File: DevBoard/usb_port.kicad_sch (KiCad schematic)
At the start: 105 parts, among them J501 TYPE-C 16PCB0.8 IP68, J502 I2CC logic analyzer, Q501 IAUC45N04S6L063H, Q502 IAUC45N04S6L063H, U501 TPS25751DREFR, U502 M24512-DFMC6TG, U503 BQ25756RRVR, U504 TPS62933DRLR

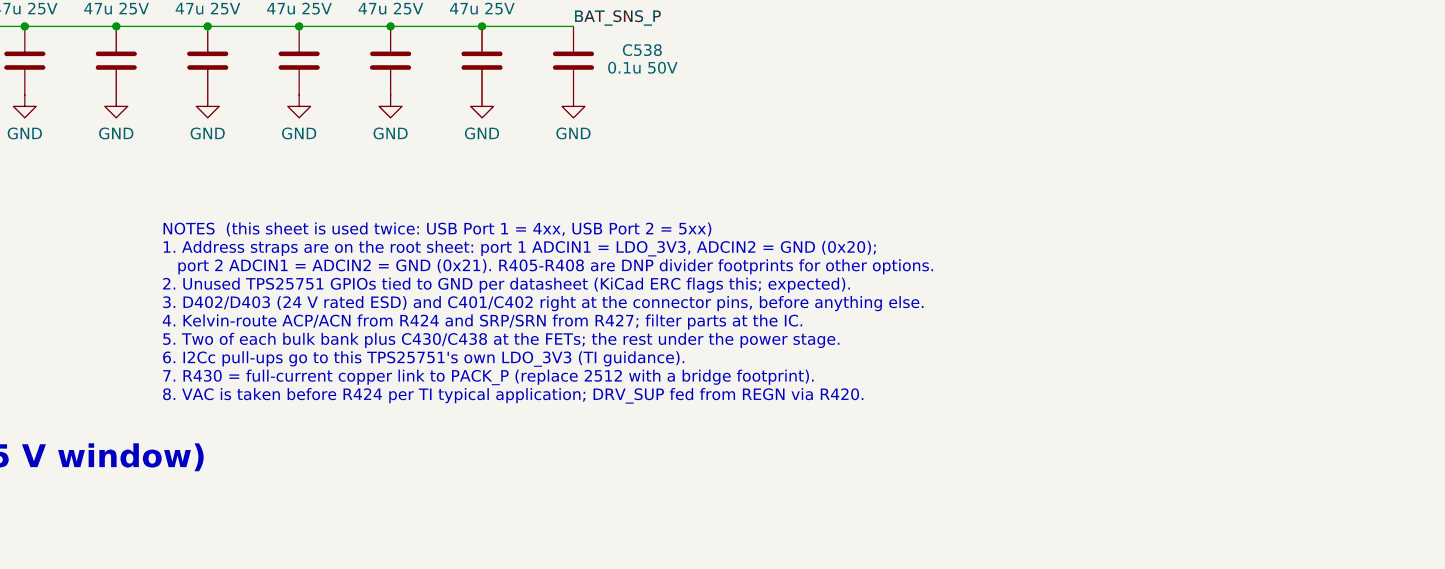
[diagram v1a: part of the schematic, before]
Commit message: Dev board: hand-solder the INA190s, keep PPHV bulk with soft-start
- U201/U202 sourced from DigiKey/Mouser and hand-soldered: excluded from the
  position file, LCSC removed, MPN and Sourcing properties added, sheet note
- PPHV bulk above 100 uF justified by the TPS25751D sink soft-start (inrush
  ~0.1 A at setting 0); sheet note asks for SS setting 0 or 1 in config
- README and circuit description updated

Co-Authored-By: Claude Opus 5.5 <noreply@anthropic.com>
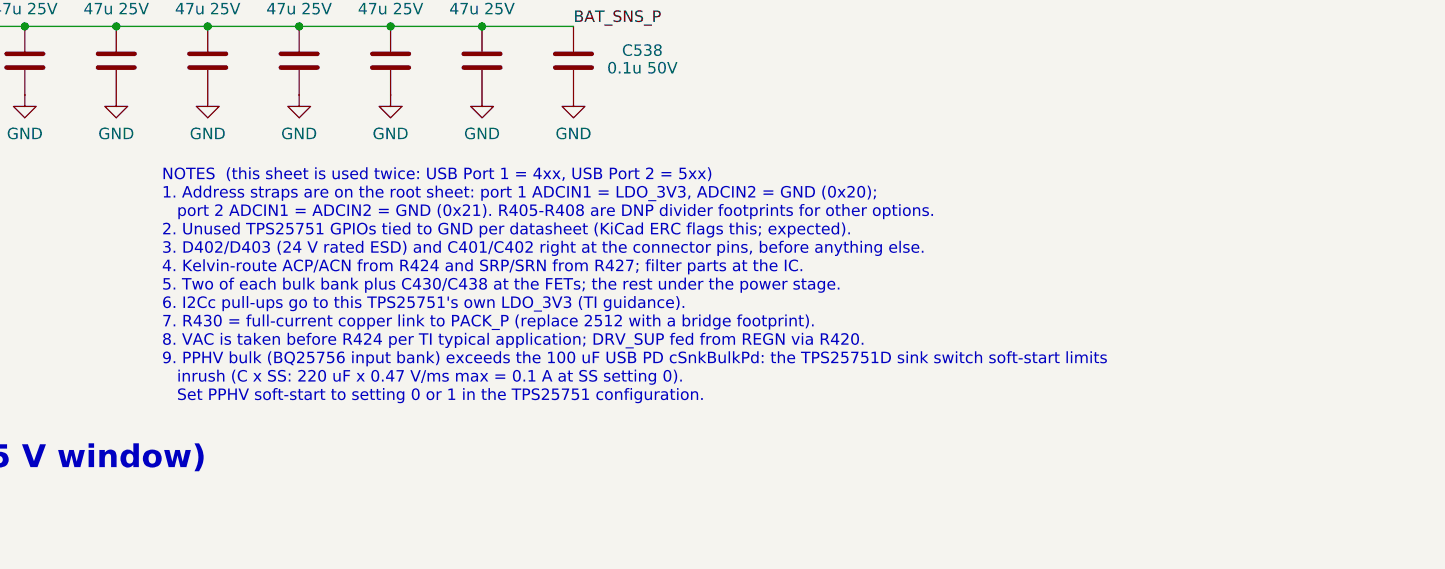
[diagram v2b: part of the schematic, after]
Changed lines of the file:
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@@
 		)
 	)
-	(text "NOTES  (this sheet is used twice: USB Port 1 = 4xx, USB Port 2 = 5xx)\n1. Address straps are on the root sheet: port 1 ADCIN1 = LDO_3V3, ADCIN2 = GND (0x20);\n   port 2 ADCIN1 = ADCIN2 = GND (0x21). R405-R408 are DNP divider footprints for other options.\n2. Unused TPS25751 GPIOs tied to GND per datasheet (KiCad ERC flags this; expected).\n3. D402/D403 (24 V rated ESD) and C401/C402 right at the connector pins, before anything else.\n4. Kelvin-route ACP/ACN from R424 and SRP/SRN from R427; filter parts at the IC.\n5. Two of each bulk bank plus C430/C438 at the FETs; the rest under the power stage.\n6. I2Cc pull-ups go to this TPS25751's own LDO_3V3 (TI guidance).\n7. R430 = full-current copper link to PACK_P (replace 2512 with a bridge footprint).\n8. VAC is taken before R424 per TI typical application; DRV_SUP fed from REGN via R420."
+	(text "NOTES  (this sheet is used twice: USB Port 1 = 4xx, USB Port 2 = 5xx)\n1. Address straps are on the root sheet: port 1 ADCIN1 = LDO_3V3, ADCIN2 = GND (0x20);\n   port 2 ADCIN1 = ADCIN2 = GND (0x21). R405-R408 are DNP divider footprints for other options.\n2. Unused TPS25751 GPIOs tied to GND per datasheet (KiCad ERC flags this; expected).\n3. D402/D403 (24 V rated ESD) and C401/C402 right at the connector pins, before anything else.\n4. Kelvin-route ACP/ACN from R424 and SRP/SRN from R427; filter parts at the IC.\n5. Two of each bulk bank plus C430/C438 at the FETs; the rest under the power stage.\n6. I2Cc pull-ups go to this TPS25751's own LDO_3V3 (TI guidance).\n7. R430 = full-current copper link to PACK_P (replace 2512 with a bridge footprint).\n8. VAC is taken before R424 per TI typical application; DRV_SUP fed from REGN via R420.\n9. PPHV bulk (BQ25756 input bank) exceeds the 100 uF USB PD cSnkBulkPd: the TPS25751D sink switch soft-start limits\n   inrush (C x SS: 220 uF x 0.47 V/ms max = 0.1 A at SS setting 0).\n   Set PPHV soft-start to setting 0 or 1 in the TPS25751 configuration."
 		(exclude_from_sim no)
 		(at 459.74 160.02 0)
@@
 		(dnp no)
 		(property "Reference" "C546"
-			(at 76.20 191.68 0)
+			(at 76.2 191.68 0)
 			(show_name no)
 			(do_not_autoplace no)
@@
 		)
 		(property "Value" "0.1u 50V"
-			(at 76.20 193.65 0)
+			(at 76.2 193.65 0)
 			(show_name no)
 			(do_not_autoplace no)
@@
 		(dnp no)
 		(property "Reference" "C525"
-			(at 368.30 114.21 0)
+			(at 368.3 114.21 0)
 			(show_name no)
 			(do_not_autoplace no)
@@
 		)
 		(property "Value" "22u 35V"
-			(at 368.30 116.18 0)
+			(at 368.3 116.18 0)
 			(show_name no)
 			(do_not_autoplace no)
@@
 		(dnp no)
 		(property "Reference" "C543"
-			(at 157.48 199.30 0)
+			(at 157.48 199.3 0)
 			(show_name no)
 			(do_not_autoplace no)
@@
 		(dnp no)
 		(property "Reference" "C541"
-			(at 137.16 199.30 0)
+			(at 137.16 199.3 0)
 			(show_name no)
 			(do_not_autoplace no)
@@
 		)
 		(property "Value" "3V3"
-			(at 317.50 192.53 0)
+			(at 317.5 192.53 0)
 			(show_name no)
 			(do_not_autoplace no)
@@
 		)
 		(property "Value" "GND"
-			(at 38.10 123.70 0)
+			(at 38.1 123.7 0)
 			(show_name no)
 			(do_not_autoplace no)
@@
 		)
 		(property "Value" "GND"
-			(at 266.70 161.80 0)
+			(at 266.7 161.8 0)
 			(show_name no)
 			(do_not_autoplace no)
@@
 		)
 		(property "Value" "GND"
-			(at 456.00 99.06 0)
+			(at 456 99.06 0)
 			(show_name no)
 			(do_not_autoplace no)
@@
 		(dnp no)
 		(property "Reference" "U503"
-			(at 381.00 174.05 0)
+			(at 381 174.05 0)
 			(show_name no)
 			(do_not_autoplace no)
@@
 		)
 		(property "Value" "BQ25756RRVR"
-			(at 381.00 176.02 0)
+			(at 381 176.02 0)
 			(show_name no)
 			(do_not_autoplace no)
@@
 		)
 		(property "Value" "GND"
-			(at 45.72 123.70 0)
+			(at 45.72 123.7 0)
 			(show_name no)
 			(do_not_autoplace no)
@@
 		(dnp no)
 		(property "Reference" "R519"
-			(at 419.33 213.50 0)
+			(at 419.33 213.5 0)
 			(show_name no)
 			(do_not_autoplace no)
@@
 		(dnp no)
 		(property "Reference" "U504"
-			(at 101.60 189.29 0)
+			(at 101.6 189.29 0)
 			(show_name no)
 			(do_not_autoplace no)
@@
 		)
 		(property "Value" "TPS62933DRLR"
-			(at 101.60 191.26 0)
+			(at 101.6 191.26 0)
 			(show_name no)
 			(do_not_autoplace no)
@@
 		)
 		(property "Value" "GND"
-			(at 76.20 229.11 0)
+			(at 76.2 229.11 0)
 			(show_name no)
 			(do_not_autoplace no)
@@
 		(dnp no)
 		(property "Reference" "C530"
-			(at 419.10 114.21 0)
+			(at 419.1 114.21 0)
 			(show_name no)
 			(do_not_autoplace no)
@@
 		)
 		(property "Value" "0.1u 50V"
-			(at 419.10 116.18 0)
+			(at 419.1 116.18 0)
 			(show_name no)
 			(do_not_autoplace no)
@@
 		(dnp no)
 		(property "Reference" "C532"
-			(at 444.50 114.21 0)
+			(at 444.5 114.21 0)
 			(show_name no)
 			(do_not_autoplace no)
@@
 		)
 		(property "Value" "47u 25V"
-			(at 444.50 116.18 0)
+			(at 444.5 116.18 0)
 			(show_name no)
 			(do_not_autoplace no)
@@
 		)
 		(property "Value" "GND"
-			(at 368.30 130.05 0)
+			(at 368.3 130.05 0)
 			(show_name no)
 			(do_not_autoplace no)
@@
 		(dnp no)
 		(property "Reference" "C517"
-			(at 458.20 85.38 90)
+			(at 458.2 85.38 90)
 			(show_name no)
 			(do_not_autoplace no)
@@
 		)
 		(property "Value" "0.47u 25V"
-			(at 458.20 87.34 90)
+			(at 458.2 87.34 90)
 			(show_name no)
 			(do_not_autoplace no)
@@
 		)
 		(property "Value" "GND"
-			(at 363.22 85.60 0)
+			(at 363.22 85.6 0)
 			(show_name no)
 			(do_not_autoplace no)
@@
 		(dnp no)
 		(property "Reference" "J502"
-			(at 284.48 161.80 0)
+			(at 284.48 161.8 0)
 			(show_name no)
 			(do_not_autoplace no)
@@
 		)
 		(property "Value" "GND"
-			(at 495.30 130.05 0)
+			(at 495.3 130.05 0)
 			(show_name no)
 			(do_not_autoplace no)
@@
 		)
 		(property "Value" "GND"
-			(at 317.50 130.05 0)
+			(at 317.5 130.05 0)
 			(show_name no)
 			(do_not_autoplace no)
@@
 		(dnp no)
 		(property "Reference" "R511"
-			(at 342.67 200.80 0)
+			(at 342.67 200.8 0)
 			(show_name no)
 			(do_not_autoplace no)
@@
 		(dnp no)
 		(property "Reference" "C537"
-			(at 495.30 114.21 0)
+			(at 495.3 114.21 0)
 			(show_name no)
 			(do_not_autoplace no)
@@
 		)
 		(property "Value" "47u 25V"
-			(at 495.30 116.18 0)
+			(at 495.3 116.18 0)
 			(show_name no)
 			(do_not_autoplace no)
@@
 		)
 		(property "Value" "GND"
-			(at 254.00 164.34 0)
+			(at 254 164.34 0)
 			(show_name no)
 			(do_not_autoplace no)
@@
 		)
 		(property "Value" "GND"
-			(at 354.40 208.28 0)
+			(at 354.4 208.28 0)
 			(show_name no)
 			(do_not_autoplace no)
@@
 		)
 		(property "Value" "IAUC45N04S6L063H"
-			(at 350.52 66.80 0)
+			(at 350.52 66.8 0)
 			(show_name no)
 			(do_not_autoplace no)
@@
 		)
 		(property "Value" "PWR_FLAG"
-			(at 228.60 285.24 0)
+			(at 228.6 285.24 0)
 			(show_name no)
 			(do_not_autoplace no)
@@
 		(dnp no)
 		(property "Reference" "R513"
-			(at 353.06 244.20 0)
+			(at 353.06 244.2 0)
 			(show_name no)
 			(do_not_autoplace no)
@@
 		(dnp no)
 		(property "Reference" "Q502"
-			(at 419.10 64.83 0)
+			(at 419.1 64.83 0)
 			(show_name no)
 			(do_not_autoplace no)
@@
 		)
 		(property "Value" "IAUC45N04S6L063H"
-			(at 419.10 66.80 0)
+			(at 419.1 66.8 0)
 			(show_name no)
 			(do_not_autoplace no)
@@
 		)
 		(property "Value" "10k B3435"
-			(at 410.78 238.10 0)
+			(at 410.78 238.1 0)
 			(show_name no)
 			(do_not_autoplace no)
@@
 		(dnp no)
 		(property "Reference" "C540"
-			(at 114.30 204.83 0)
+			(at 114.3 204.83 0)
 			(show_name no)
 			(do_not_autoplace no)
@@
 		)
 		(property "Value" "0.1u 25V"
-			(at 114.30 206.80 0)
+			(at 114.3 206.8 0)
 			(show_name no)
 			(do_not_autoplace no)
@@
 		)
 		(property "Value" "GND"
-			(at 406.40 85.60 0)
+			(at 406.4 85.6 0)
 			(show_name no)
 			(do_not_autoplace no)
@@
 		)
 		(property "Value" "GND"
-			(at 444.50 130.05 0)
+			(at 444.5 130.05 0)
 			(show_name no)
 			(do_not_autoplace no)
@@
 		)
 		(property "Value" "GND"
-			(at 76.20 207.52 0)
+			(at 76.2 207.52 0)
 			(show_name no)
 			(do_not_autoplace no)
@@
 		(dnp no)
 		(property "Reference" "C512"
-			(at 406.40 173.90 0)
+			(at 406.4 173.9 0)
 			(show_name no)
 			(do_not_autoplace no)
@@
 		)
 		(property "Value" "0.1u 25V"
-			(at 406.40 175.87 0)
+			(at 406.4 175.87 0)
 			(show_name no)
 			(do_not_autoplace no)
@@
 		(dnp no)
 		(property "Reference" "TP503"
-			(at 76.20 283.71 0)
+			(at 76.2 283.71 0)
 			(show_name no)
 			(do_not_autoplace no)
@@
 		(dnp no)
 		(property "Reference" "C542"
-			(at 147.32 199.30 0)
+			(at 147.32 199.3 0)
 			(show_name no)
 			(do_not_autoplace no)
@@
 		)
 		(property "Value" "GND"
-			(at 356.94 241.30 0)
+			(at 356.94 241.3 0)
 			(show_name no)
 			(do_not_autoplace no)
@@
 		)
 		(property "Value" "GND"
-			(at 342.90 244.35 0)
+			(at 342.9 244.35 0)
 			(show_name no)
 			(do_not_autoplace no)
@@
 		)
 		(property "Value" "GND"
-			(at 238.76 161.80 0)
+			(at 238.76 161.8 0)
 			(show_name no)
 			(do_not_autoplace no)
@@
 		)
 		(property "Value" "GND"
-			(at 101.60 220.22 0)
+			(at 101.6 220.22 0)
 			(show_name no)
 			(do_not_autoplace no)
@@
 		(dnp no)
 		(property "Reference" "TP508"
-			(at 152.40 283.71 0)
+			(at 152.4 283.71 0)
 			(show_name no)
 			(do_not_autoplace no)
@@
 		)
 		(property "Value" "GND"
-			(at 419.10 130.05 0)
+			(at 419.1 130.05 0)
 			(show_name no)
 			(do_not_autoplace no)

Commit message: Dev board: project footprints for holder, USB-C, half-bridge, module, EEPROM, BQ25756
- tools/make_footprints.py generates MonolithDev.pretty from the datasheets:
  BH-21700-B1BJ001 holder, Shou Han USB-C (with board-edge cutout),
  Infineon PG-TDSON-8-57 half-bridge (land + stencil), STM32WB1MMC LGA77,
  ST UFDFPN8 2x3 with the correct 1.2x1.4 exposed pad, and a 10 A net tie
- BQ25756 RRV0036A footprint from Antmicro (Apache-2.0), checked against TI
- Footprints assigned; R430/R530 become net-tie links, off the BOM and CPL
- Every symbol pin has a pad and vice versa; nets, ERC and overlaps unchanged

Co-Authored-By: Claude Opus 5.5 <noreply@anthropic.com>
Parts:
- J501: footprint (none) -> MonolithDev:USB_C_Receptacle_ShouHan_TYPE-C_16PCB0.8_IP68
- Q501, Q502: footprint (none) -> MonolithDev:Infineon_PG-TDSON-8-57_HalfBridge
- R530: value 0R copper link -> Link 10A; footprint Resistor_SMD:R_2512_6332Metric -> MonolithDev:NetTie-2_SMD_3x3mm_Bridge3mm; Notes full current -> copper link (net tie footprint), not a part; keeps VBAT_SYS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; now left out of the parts list
- U502: footprint Package_DFN_QFN:DFN-8-1EP_2x3mm_P0.5mm_EP0.61x2.2mm -> MonolithDev:ST_UFDFPN-8-1EP_2x3mm_P0.5mm_EP1.2x1.4mm
- U503: footprint (none) -> MonolithDev:TI_VQFN-36-1EP_RRV0036A_5x6mm_P0.5mm
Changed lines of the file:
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@@
 		)
 	)
-	(text "NOTES  (this sheet is used twice: USB Port 1 = 4xx, USB Port 2 = 5xx)\n1. Address straps are on the root sheet: port 1 ADCIN1 = LDO_3V3, ADCIN2 = GND (0x20);\n   port 2 ADCIN1 = ADCIN2 = GND (0x21). R405-R408 are DNP divider footprints for other options.\n2. Unused TPS25751 GPIOs tied to GND per datasheet (KiCad ERC flags this; expected).\n3. D402/D403 (24 V rated ESD) and C401/C402 right at the connector pins, before anything else.\n4. Kelvin-route ACP/ACN from R424 and SRP/SRN from R427; filter parts at the IC.\n5. Two of each bulk bank plus C430/C438 at the FETs; the rest under the power stage.\n6. I2Cc pull-ups go to this TPS25751's own LDO_3V3 (TI guidance).\n7. R430 = full-current copper link to PACK_P (replace 2512 with a bridge footprint).\n8. VAC is taken before R424 per TI typical application; DRV_SUP fed from REGN via R420.\n9. PPHV bulk (BQ25756 input bank) exceeds the 100 uF USB PD cSnkBulkPd: the TPS25751D sink switch soft-start limits\n   inrush (C x SS: 220 uF x 0.47 V/ms max = 0.1 A at SS setting 0).\n   Set PPHV soft-start to setting 0 or 1 in the TPS25751 configuration."
+	(text "NOTES  (this sheet is used twice: USB Port 1 = 4xx, USB Port 2 = 5xx)\n1. Address straps are on the root sheet: port 1 ADCIN1 = LDO_3V3, ADCIN2 = GND (0x20);\n   port 2 ADCIN1 = ADCIN2 = GND (0x21). R405-R408 are DNP divider footprints for other options.\n2. Unused TPS25751 GPIOs tied to GND per datasheet (KiCad ERC flags this; expected).\n3. D402/D403 (24 V rated ESD) and C401/C402 right at the connector pins, before anything else.\n4. Kelvin-route ACP/ACN from R424 and SRP/SRN from R427; filter parts at the IC.\n5. Two of each bulk bank plus C430/C438 at the FETs; the rest under the power stage.\n6. I2Cc pull-ups go to this TPS25751's own LDO_3V3 (TI guidance).\n7. R430 = 10 A copper link to PACK_P (net-tie footprint, not a part); widen with zones.\n8. VAC is taken before R424 per TI typical application; DRV_SUP fed from REGN via R420.\n9. PPHV bulk (BQ25756 input bank) exceeds the 100 uF USB PD cSnkBulkPd: the TPS25751D sink switch soft-start limits\n   inrush (C x SS: 220 uF x 0.47 V/ms max = 0.1 A at SS setting 0).\n   Set PPHV soft-start to setting 0 or 1 in the TPS25751 configuration."
 		(exclude_from_sim no)
 		(at 459.74 160.02 0)
@@
 			)
 		)
-		(property "Footprint" "Package_DFN_QFN:DFN-8-1EP_2x3mm_P0.5mm_EP0.61x2.2mm"
+		(property "Footprint" "MonolithDev:ST_UFDFPN-8-1EP_2x3mm_P0.5mm_EP1.2x1.4mm"
 			(at 254 152.4 0)
 			(hide yes)
@@
 			)
 		)
-		(property "Footprint" ""
+		(property "Footprint" "MonolithDev:TI_VQFN-36-1EP_RRV0036A_5x6mm_P0.5mm"
 			(at 381 203.2 0)
 			(hide yes)
@@
 		(body_style 1)
 		(exclude_from_sim no)
-		(in_bom yes)
+		(in_bom no)
 		(on_board yes)
-		(in_pos_files yes)
+		(in_pos_files no)
 		(dnp no)
 		(property "Reference" "R530"
@@
 			)
 		)
-		(property "Value" "0R copper link"
+		(property "Value" "Link 10A"
 			(at 474.83 58.16 90)
 			(show_name no)
@@
 			)
 		)
-		(property "Footprint" "Resistor_SMD:R_2512_6332Metric"
+		(property "Footprint" "MonolithDev:NetTie-2_SMD_3x3mm_Bridge3mm"
 			(at 474.98 62.738 90)
 			(hide yes)
@@
 			)
 		)
-		(property "Notes" "full current"
+		(property "Notes" "copper link (net tie footprint), not a part; keeps VBAT_SYS and PACK_P as separate net names"
 			(at 0 0 0)
 			(hide yes)
@@
 			)
 		)
-		(property "Footprint" ""
+		(property "Footprint" "MonolithDev:Infineon_PG-TDSON-8-57_HalfBridge"
 			(at 350.52 73.66 0)
 			(hide yes)
@@
 			)
 		)
-		(property "Footprint" ""
+		(property "Footprint" "MonolithDev:Infineon_PG-TDSON-8-57_HalfBridge"
 			(at 419.1 73.66 0)
 			(hide yes)
@@
 			)
 		)
-		(property "Footprint" ""
+		(property "Footprint" "MonolithDev:USB_C_Receptacle_ShouHan_TYPE-C_16PCB0.8_IP68"
 			(at 49.53 96.52 0)
 			(hide yes)

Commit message: Dev board: first-pass placement (196x115), DRC clean before routing
- tools/place_parts.py: mechanical (outline, holes, USB-C), hand placement of
  holders, gauge core and VC filter ladder, sleep-current section, MCU and
  both charger power trains; auto placement of the small parts next to the
  pins they serve; silkscreen labels (P1/P2 test points, USB 1/2)
- Board widened to 196 mm: holder courtyards collided with the corner holes
- TPS25751 footprint copy with the PPHV/VBUS pad gap opened to 0.15 mm (2 oz)
- Rules: HighCurrent/Power pad clearance 0.15 mm; 0.25 mm only between
  high-current copper and small-signal copper
- DRC: 0 placement/clearance/silk issues, 0 parity issues; unrouted only

Co-Authored-By: Claude Opus 5.5 <noreply@anthropic.com>
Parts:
- U501: footprint Package_DFN_QFN:Texas_REF0038A_WQFN-38-2EP_6x4mm_P0.4 -> MonolithDev:TI_WQFN-38-2EP_REF0038A_6x4mm_P0.4mm_2oz
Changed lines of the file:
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@@
 			)
 		)
-		(property "Footprint" "Package_DFN_QFN:Texas_REF0038A_WQFN-38-2EP_6x4mm_P0.4"
+		(property "Footprint" "MonolithDev:TI_WQFN-38-2EP_REF0038A_6x4mm_P0.4mm_2oz"
 			(at 170.18 58.42 0)
 			(hide yes)
